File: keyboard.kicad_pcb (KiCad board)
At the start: 2 copper layers, 108.2 x 96.2 mm, 68 parts, among them J2 TYPE-C-31-M-12, U1 ATmega32U4-A, Y1 Crystal_GND24_Small

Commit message: fixFlip
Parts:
- Key_+1, Key_enter1: footprint Button_Switch_Keyboard:MX-Hotswap-2U-Vertical-ReversedStabilizers -> Button_Switch_Keyboard:MX-Hotswap-2U-ReversedStabilizers
- turned Key_+1 to -90 degrees
- turned Key_enter1 to -90 degrees
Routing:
- net Y3: track 79.1 -> 102.4 mm
- net Net-(D12-A): track 2.45 -> 15.7 mm, vias 0 -> 2
- net Net-(D16-A): track 2.51 -> 14.0 mm

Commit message: V2-led
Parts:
- added C10: C_Small, Capacitor_SMD:C_0805_2012Metric, B.Cu at (225.5, 77.4)
- added C11: C_Small, Capacitor_SMD:C_0805_2012Metric, B.Cu at (206.4, 77.6)
- added C12: C_Small, Capacitor_SMD:C_0805_2012Metric, B.Cu at (187.3, 77.6)
- added C13: C_Small, Capacitor_SMD:C_0805_2012Metric, B.Cu at (168.2, 77.6)
- added C14: C_Small, Capacitor_SMD:C_0805_2012Metric, B.Cu at (168.3, 96.9)
- added C15: C_Small, Capacitor_SMD:C_0805_2012Metric, B.Cu at (187.3, 96.9)
- added C16: C_Small, Capacitor_SMD:C_0805_2012Metric, B.Cu at (206.5, 96.8)
- added C17: C_Small, Capacitor_SMD:C_0805_2012Metric, B.Cu at (227.6, 95.5)
- added C18: C_Small, Capacitor_SMD:C_0805_2012Metric, B.Cu at (256.3, 96.8)
- added C19: C_Small, Capacitor_SMD:C_0805_2012Metric, B.Cu at (168.3, 115.7)
- added C20: C_Small, Capacitor_SMD:C_0805_2012Metric, B.Cu at (187.5, 115.6)
- added C21: C_Small, Capacitor_SMD:C_0805_2012Metric, B.Cu at (256.4, 115.7)
- added C22: C_Small, Capacitor_SMD:C_0805_2012Metric, B.Cu at (256.4, 134.9)
- added C23: C_Small, Capacitor_SMD:C_0805_2012Metric, B.Cu at (233.5, 136.5)
- added C24: C_Small, Capacitor_SMD:C_0805_2012Metric, B.Cu at (206.4, 135.0)
- added C25: C_Small, Capacitor_SMD:C_0805_2012Metric, B.Cu at (186.7, 134.9)
- added C26: 10uf, Capacitor_SMD:C_0805_2012Metric, B.Cu at (245.7, 82.3)
- added C27: C_Small, Capacitor_SMD:C_0805_2012Metric, B.Cu at (206.4, 115.7)
- added C28: C_Small, Capacitor_SMD:C_0805_2012Metric, B.Cu at (169.1, 135.0)
- added C29: C_Small, Capacitor_SMD:C_0805_2012Metric, B.Cu at (177.7, 153.7)
- added C30: C_Small, Capacitor_SMD:C_0805_2012Metric, B.Cu at (206.4, 153.7)
- added C31: C_Small, Capacitor_SMD:C_0805_2012Metric, B.Cu at (256.4, 153.8)
- added C9: C_Small, Capacitor_SMD:C_0805_2012Metric, B.Cu at (256.3, 77.8)
- added R5: 500, Resistor_SMD:R_0805_2012Metric, B.Cu at (261.2, 77.5)
- added U10: ~, MyLiB:MX-SK-E-Right_Left, F.Cu at (225.4, 98.4)
- added U11: ~, MyLiB:MX-SK-E-Right_Left, F.Cu at (256.4, 88.9)
- added U12: ~, MyLiB:MX-SK-E-Left_Right, F.Cu at (256.4, 108.0)
- added U13: ~, MyLiB:MX-SK-E-Left_Right, F.Cu at (206.4, 107.9)
- added U14: ~, MyLiB:MX-SK-E-Left_Right, F.Cu at (187.3, 108.0)
- added U15: ~, MyLiB:MX-SK-E-Left_Right, F.Cu at (168.3, 107.9)
- added U16: ~, MyLiB:MX-SK-E-Right_Left, F.Cu at (168.3, 127.0)
- added U17: ~, MyLiB:MX-SK-E-Right_Left, F.Cu at (187.3, 127.0)
- added U18: ~, MyLiB:MX-SK-E-Right_Left, F.Cu at (206.4, 127.0)
- added U2: ~, MyLiB:MX-SK-E-Left_Right, F.Cu at (256.4, 69.8)
- added U20: ~, MyLiB:MX-SK-E-Right_Left, F.Cu at (225.4, 136.5)
- added U21: ~, MyLiB:MX-SK-E-Right_Left, F.Cu at (256.4, 127.0)
- added U22: ~, MyLiB:MX-SK-E-Left_Right, F.Cu at (256.4, 146.1)
- added U23: ~, MyLiB:MX-SK-E-Left_Right, F.Cu at (206.4, 146.0)
- added U24: ~, MyLiB:MX-SK-E-Left_Right, F.Cu at (177.8, 146.0)
- added U3: ~, MyLiB:MX-SK-E-Left_Right, F.Cu at (225.4, 69.8)
- added U4: ~, MyLiB:MX-SK-E-Left_Right, F.Cu at (206.4, 69.8)
- added U5: ~, MyLiB:MX-SK-E-Left_Right, F.Cu at (187.3, 69.8)
- added U6: ~, MyLiB:MX-SK-E-Left_Right, F.Cu at (168.3, 69.8)
- added U7: ~, MyLiB:MX-SK-E-Right_Left, F.Cu at (168.3, 88.9)
- added U8: ~, MyLiB:MX-SK-E-Right_Left, F.Cu at (187.3, 88.9)
- added U9: ~, MyLiB:MX-SK-E-Right_Left, F.Cu at (206.4, 88.9)
- moved GND1 6.64 mm to (246.9, 78.9)
- moved 5V+2 4.02 mm to (244.4, 79.0)
- moved D12 3.80 mm to (217.0, 95.9)
- moved D17 3.28 mm to (248.4, 74.5)
- moved D1 3.19 mm to (160.3, 74.6)
- moved D10 3.19 mm to (198.4, 93.7)
- moved D11 3.19 mm to (217.5, 74.6)
- moved D13 3.19 mm to (198.4, 112.7)
- moved D14 3.19 mm to (198.4, 131.8)
- moved D19 3.19 mm to (249.2, 113.5)
- moved D2 3.19 mm to (179.4, 74.6)
- moved D20 3.19 mm to (248.4, 131.7)
- moved D21 3.19 mm to (169.8, 150.8)
- moved D23 3.19 mm to (198.4, 150.8)
- moved D25 3.19 mm to (248.4, 150.8)
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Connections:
- U1 pad 41: unconnected-(U1-PF0-Pad41) -> Net-(U1-PF0)
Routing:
- net GND: track 170.0 -> 912.4 mm, vias 4 -> 40
- net +5V: track 98.7 -> 817.1 mm, vias 5 -> 73
- net Net-(U12-DOUT): track 0.00 -> 45.1 mm, vias 0 -> 4
- net Net-(U22-DOUT): track 0.00 -> 45.0 mm
- net Net-(U2-DOUT): track 0.00 -> 31.1 mm, vias 0 -> 4
- net LED_DATA_2: track 0.00 -> 28.3 mm, vias 0 -> 2
- net Net-(U1-PF0): track 0.00 -> 28.1 mm, vias 0 -> 2
- net Net-(U10-DIN): track 0.00 -> 27.4 mm, vias 0 -> 4
- net LED_DATA_1: track 0.00 -> 26.9 mm, vias 0 -> 2
- net Net-(U20-DOUT): track 0.00 -> 26.1 mm, vias 0 -> 2
- net X3: track 130.7 -> 156.2 mm, vias 2 -> 4
- net Net-(U23-DOUT): track 0.00 -> 23.6 mm
- net Net-(U21-DOUT): track 0.00 -> 22.0 mm
- net Net-(U6-DOUT): track 0.00 -> 21.2 mm, vias 0 -> 2
- net Net-(U11-DOUT): track 0.00 -> 21.1 mm, vias 0 -> 2
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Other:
- outline, holes or cut-outs redrawn
- board text added: "Cosmic"
- board text added: "V1"

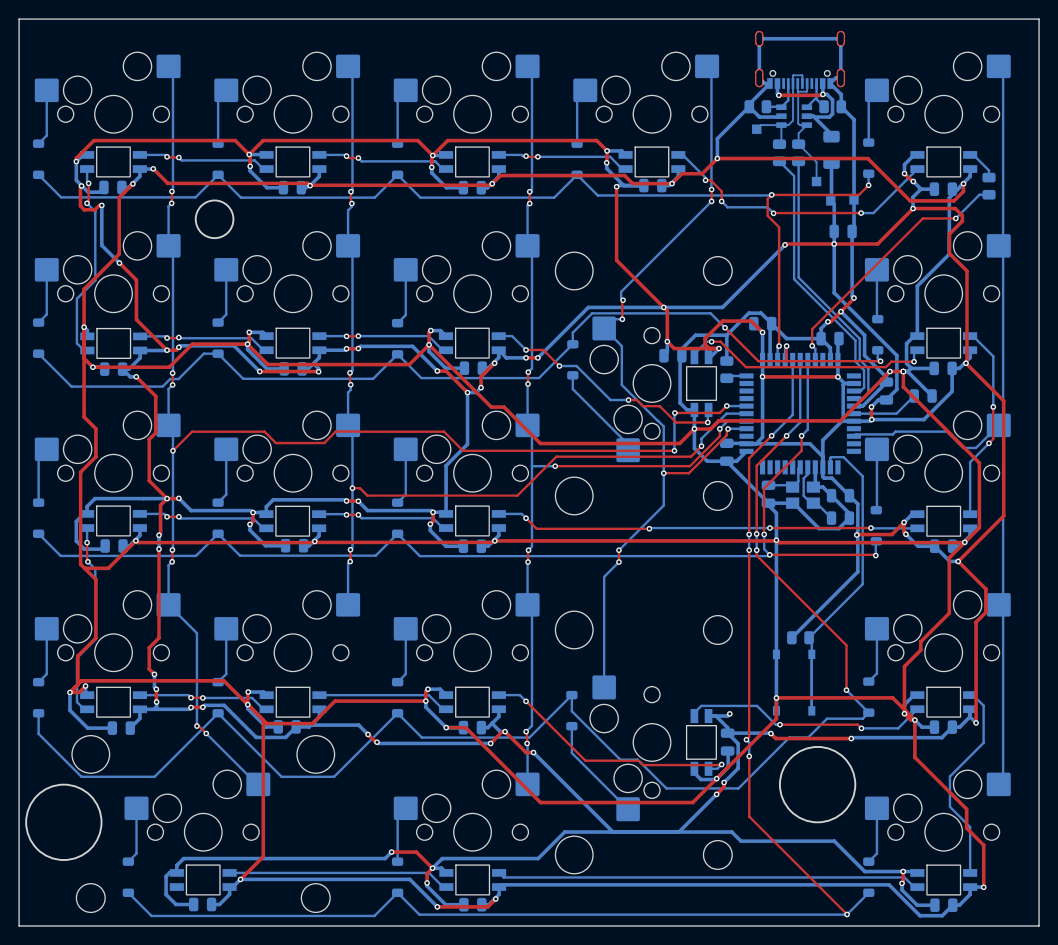
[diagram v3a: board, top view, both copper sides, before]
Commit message: V2.1, used a grounding plane
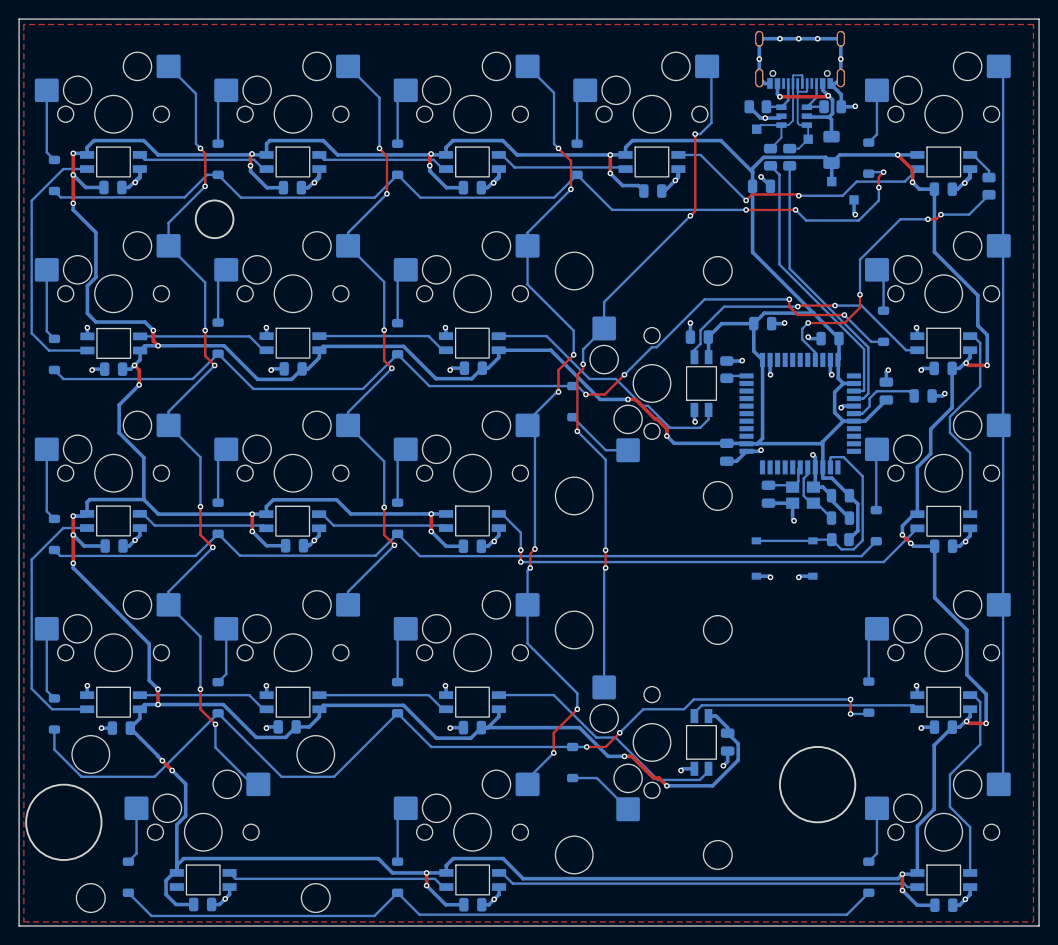
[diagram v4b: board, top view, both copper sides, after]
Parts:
- moved S2 13.2 mm to (239.5, 117.0), turned to 0 degrees
- moved R4 11.2 mm to (245.4, 115.0), turned to 180 degrees
- moved C26 9.90 mm to (237.1, 77.5)
- moved D16 5.50 mm to (217.0, 138.7)
- moved D+ 4.58 mm to (242.0, 72.5)
- moved D12 4.44 mm to (217.0, 100.3)
- moved C17 3.43 mm to (230.4, 93.5), turned to 0 degrees
- moved D3 2.40 mm to (162.0, 95.3)
- moved D5 2.40 mm to (162.0, 114.5)
- moved D1 2.40 mm to (162.0, 76.3)
- moved D6 2.40 mm to (162.0, 133.5)
- moved 5V+ 2.05 mm to (244.5, 77.0)
- moved D18 1.09 mm to (250.0, 92.3)
- moved R3 1.06 mm to (238.0, 74.4)
- moved R2 1.06 mm to (240.0, 74.4)
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- renumbered 5V+2 to 5V+, D+1 to D+, D-1 to D-, GND1 to GND
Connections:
- U1 pad 26: Y3 -> unconnected-(U1-PD6-Pad26)
- U1 pad 27: Y2 -> unconnected-(U1-PD7-Pad27)
- U1 pad 28: Y1 -> unconnected-(U1-PB4-Pad28)
- U1 pad 29: Y0 -> unconnected-(U1-PB5-Pad29)
- U1 pad 36: X0 -> unconnected-(U1-PF7-Pad36)
- U1 pad 37: X1 -> unconnected-(U1-PF6-Pad37)
- U1 pad 38: X4 -> unconnected-(U1-PF5-Pad38)
- U1 pad 39: X3 -> unconnected-(U1-PF4-Pad39)
- U1 pad 40: X2 -> unconnected-(U1-PF1-Pad40)
- U1 pad 9: Y4 -> unconnected-(U1-PB1-Pad9)
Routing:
- net GND: track 912.4 -> 134.3 mm, vias 40 -> 54
- net +5V: track 817.1 -> 723.7 mm, vias 73 -> 40
- net X4: track 147.9 -> 82.5 mm, vias 6 -> 0
- net Y0: track 149.4 -> 91.7 mm, vias 12 -> 8
- net X3: track 156.2 -> 103.3 mm
- net Y1: track 104.7 -> 68.5 mm, vias 8 -> 6
- net X2: track 118.2 -> 92.0 mm, vias 4 -> 0
- net Y4: track 95.0 -> 77.7 mm
- net Net-(U1-~{RESET}): track 38.7 -> 24.3 mm
- net X0: track 114.9 -> 100.5 mm, vias 3 -> 4
- net Y3: track 87.9 -> 73.6 mm, vias 8 -> 6
- net Y2: track 103.4 -> 89.2 mm, vias 10 -> 8
- net Net-(U6-DOUT): track 21.2 -> 28.0 mm, vias 2 -> 0
- net Net-(U15-DOUT): track 21.0 -> 27.8 mm, vias 2 -> 0
- net X1: track 105.6 -> 100.8 mm, vias 3 -> 4
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- added copper zone on F.Cu, net GND
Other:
- rule pad_to_mask_clearance: 0 -> 0.038

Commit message: upaded islands
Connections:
- U1 pad 26: unconnected-(U1-PD6-Pad26) -> Y3
- U1 pad 27: unconnected-(U1-PD7-Pad27) -> Y2
- U1 pad 28: unconnected-(U1-PB4-Pad28) -> Y1
- U1 pad 29: unconnected-(U1-PB5-Pad29) -> Y0
- U1 pad 36: unconnected-(U1-PF7-Pad36) -> X0
- U1 pad 37: unconnected-(U1-PF6-Pad37) -> X1
- U1 pad 38: unconnected-(U1-PF5-Pad38) -> X4
- U1 pad 39: unconnected-(U1-PF4-Pad39) -> X3
- U1 pad 40: unconnected-(U1-PF1-Pad40) -> X2
- U1 pad 9: unconnected-(U1-PB1-Pad9) -> Y4
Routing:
- net X4: track 82.5 -> 148.7 mm, vias 0 -> 8
- net Y0: track 91.7 -> 153.5 mm, vias 8 -> 10
- net Y1: track 68.5 -> 111.5 mm, vias 6 -> 8
- net X3: track 103.3 -> 141.9 mm, vias 4 -> 8
- net Y2: track 89.2 -> 114.1 mm, vias 8 -> 10
- net X2: track 92.0 -> 115.0 mm, vias 0 -> 2
- net X0: track 100.5 -> 119.1 mm, vias 4 -> 6
- net Y4: track 77.7 -> 95.3 mm, vias 0 -> 2
- net Y3: track 73.6 -> 89.9 mm, vias 6 -> 8
- net GND: track 134.3 -> 139.9 mm, vias 54 -> 79
- net X1: track 100.8 -> 106.3 mm, vias 4 -> 5
- net Net-(U1-PF0): track 32.6 -> 32.1 mm
- added copper zone on B.Cu, net GND

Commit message: added switch
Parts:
- added 5V+: Power, TestPoint:TestPoint_Pad_1.0x1.0mm, B.Cu at (234.2, 73.8)
- added GND: Power, TestPoint:TestPoint_Pad_1.0x1.0mm, B.Cu at (234.2, 71.4)
- added SW1: ~, MyLiB:SW-TH_MK-12D18-G040, B.Cu at (253.1, 61.6)
- moved C29 0.55 mm to (178.0, 154.2)
- moved C21 0.55 mm to (256.4, 116.2)
- moved D+ 0.53 mm to (242.1, 73.0)
- moved C25 0.49 mm to (187.0, 135.3)
- moved C30 0.49 mm to (206.7, 154.1)
- moved C24 0.49 mm to (206.7, 135.3)
- moved C22 0.49 mm to (256.7, 135.3)
- moved C31 0.49 mm to (256.7, 154.2)
- moved C28 0.49 mm to (169.4, 135.4)
- moved C20 0.43 mm to (187.5, 116.1)
- moved C19 0.39 mm to (168.4, 116.1)
- moved C27 0.35 mm to (206.4, 116.0)
- moved C18 0.35 mm to (256.3, 97.2)
- moved C12 0.32 mm to (187.2, 78.0)
- moved C13 0.31 mm to (168.2, 77.9)
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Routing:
- net +5V: track 723.8 -> 707.6 mm, vias 40 -> 38
- net GND: track 139.9 -> 147.8 mm, vias 79 -> 83
- net X2: track 115.0 -> 116.4 mm
- net X0: track 119.1 -> 120.3 mm
- net X4: track 148.7 -> 149.4 mm
- net D+: track 11.9 -> 12.4 mm

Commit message: update
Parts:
- removed 5V+ (x2), GND (x2): Power, TestPoint:TestPoint_Pad_1.0x1.0mm
- removed D+: D+, TestPoint:TestPoint_Pad_1.0x1.0mm
- removed D-: D-, TestPoint:TestPoint_Pad_1.0x1.0mm
- added 5V+2: Power, TestPoint:TestPoint_Pad_1.0x1.0mm, B.Cu at (242.1, 77.5)
- added D+1: D+, TestPoint:TestPoint_Pad_1.0x1.0mm, B.Cu at (242.2, 72.7)
- added D-1: D-, TestPoint:TestPoint_Pad_1.0x1.0mm, B.Cu at (236.8, 71.5)
- added GND1: Power, TestPoint:TestPoint_Pad_1.0x1.0mm, B.Cu at (244.5, 77.5)
- added H1: MountingHole, MountingHole:MountingHole_3.2mm_M3, F.Cu at (196.8, 79.4)
- added H2: MountingHole, MountingHole:MountingHole_3.2mm_M3, F.Cu at (196.8, 136.5)
- added H3: MountingHole, MountingHole:MountingHole_3.2mm_M3, F.Cu at (246.9, 136.5)
- added H4: MountingHole, MountingHole:MountingHole_3.2mm_M3, F.Cu at (246.9, 79.4)
- added H5: MountingHole, marbastlib-mx:STAB_MX_2u, F.Cu at (225.4, 98.4)
- added H6: MountingHole, marbastlib-mx:STAB_MX_2u, F.Cu at (225.4, 136.5)
- added H7: MountingHole, marbastlib-mx:STAB_MX_2u, F.Cu at (177.8, 146.0)
- Custom-1, Custom-2, Custom-3, Custom-4, Custom-5, Key_*1, Key_-1, Key_/1, Key_1, Key_2, Key_3, Key_4, Key_5, Key_6, Key_7, Key_8, Key_9, Key_del1, NumLock1: footprint MX_keys:MX-Hotswap-1U -> marbastlib-mx:SW_MX_HS_S_CPG151101S11_1u
- Key_+1, Key_0, Key_enter1: footprint Button_Switch_Keyboard:MX-Hotswap-2U-ReversedStabilizers -> marbastlib-mx:SW_MX_HS_S_CPG151101S11_1u
- U10, U11, U12, U13, U14, U15, U16, U17, U18, U2, U20, U21, U22, U23, U24, U3, U4, U5, U6, U7, U8, U9: moved to B.Cu
- moved C31 124.1 mm to (162.7, 73.2), turned to -90 degrees
- moved C13 109.4 mm to (261.9, 134.3), turned to 90 degrees
- moved C30 84.7 mm to (181.8, 73.2), turned to -90 degrees
- moved C29 84.1 mm to (200.8, 73.2), turned to -90 degrees
- moved C17 80.7 mm to (172.2, 149.4), turned to -90 degrees
- moved C28 80.1 mm to (219.9, 73.2), turned to -90 degrees
- moved C12 76.8 mm to (261.9, 95.9), turned to 90 degrees
- moved C18 76.2 mm to (200.8, 149.4), turned to -90 degrees
- moved C20 71.6 mm to (250.8, 149.4), turned to -90 degrees
- moved C9 71.4 mm to (211.9, 134.0), turned to 90 degrees
- moved C10 64.9 mm to (192.9, 134.1), turned to 90 degrees
- moved C11 64.8 mm to (173.8, 134.0), turned to 90 degrees
- moved C19 63.8 mm to (230.3, 131.0), turned to 0 degrees
- moved C27 61.7 mm to (250.8, 73.2), turned to -90 degrees
- moved C22 49.9 mm to (230.3, 92.9)
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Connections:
- C10 pad 2: +5V -> LEDP
- C11 pad 2: +5V -> LEDP
- C12 pad 2: +5V -> LEDP
- C13 pad 2: +5V -> LEDP
- C14 pad 2: +5V -> LEDP
- C15 pad 2: +5V -> LEDP
- C16 pad 2: +5V -> LEDP
- C17 pad 2: +5V -> LEDP
- C18 pad 2: +5V -> LEDP
- C19 pad 2: +5V -> LEDP
- C20 pad 2: +5V -> LEDP
- C21 pad 2: +5V -> LEDP
- C22 pad 2: +5V -> LEDP
- C23 pad 2: +5V -> LEDP
- C24 pad 2: +5V -> LEDP
- C25 pad 2: +5V -> LEDP
- C27 pad 2: +5V -> LEDP
- C28 pad 2: +5V -> LEDP
- C29 pad 2: +5V -> LEDP
- C30 pad 2: +5V -> LEDP
- C31 pad 2: +5V -> LEDP
- C9 pad 2: +5V -> LEDP
- D12 pad 1: X1 -> X2
- D16 pad 1: X3 -> X4
- SW1 pad 2: +5V -> LEDP
- U10 pad 1: +5V -> LEDP
- U11 pad 1: +5V -> LEDP
- U12 pad 1: +5V -> LEDP
- U13 pad 1: +5V -> LEDP
- U14 pad 1: +5V -> LEDP
- U15 pad 1: +5V -> LEDP
- U16 pad 1: +5V -> LEDP
- U17 pad 1: +5V -> LEDP
- U18 pad 1: +5V -> LEDP
- U2 pad 1: +5V -> LEDP
- U20 pad 1: +5V -> LEDP
- U21 pad 1: +5V -> LEDP
- U22 pad 1: +5V -> LEDP
- U23 pad 1: +5V -> LEDP
- U24 pad 1: +5V -> LEDP
- U3 pad 1: +5V -> LEDP
- U4 pad 1: +5V -> LEDP
- U5 pad 1: +5V -> LEDP
- U6 pad 1: +5V -> LEDP
- U7 pad 1: +5V -> LEDP
- U8 pad 1: +5V -> LEDP
- U9 pad 1: +5V -> LEDP
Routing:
- net LEDP: track 0.00 -> 688.6 mm, vias 0 -> 14
- net +5V: track 707.6 -> 104.1 mm, vias 38 -> 2
- net GND: track 147.8 -> 121.9 mm, vias 83 -> 17
- net LED_DATA_IN: track 3.70 -> 27.1 mm
- net X3: track 141.9 -> 123.1 mm, vias 8 -> 2
- net Net-(U1-PF0): track 32.1 -> 14.7 mm, vias 4 -> 2
- net X2: track 116.4 -> 128.5 mm
- net Y2: track 114.1 -> 104.3 mm, vias 10 -> 2
- net X1: track 106.6 -> 97.3 mm, vias 5 -> 2
- net X0: track 120.3 -> 115.0 mm, vias 6 -> 3
- net X4: track 149.4 -> 144.3 mm, vias 8 -> 2
- net Net-(D1-A): track 7.73 -> 2.83 mm
- net Net-(D6-A): track 7.73 -> 2.83 mm
- net Net-(D3-A): track 7.66 -> 2.77 mm
- net Net-(U1-UCAP): track 8.09 -> 3.21 mm
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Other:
- outline, holes or cut-outs redrawn
- rule pad_to_mask_clearance: 0.038 -> 0
